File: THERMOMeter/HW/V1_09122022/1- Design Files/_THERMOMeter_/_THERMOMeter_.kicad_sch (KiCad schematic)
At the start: 0 parts

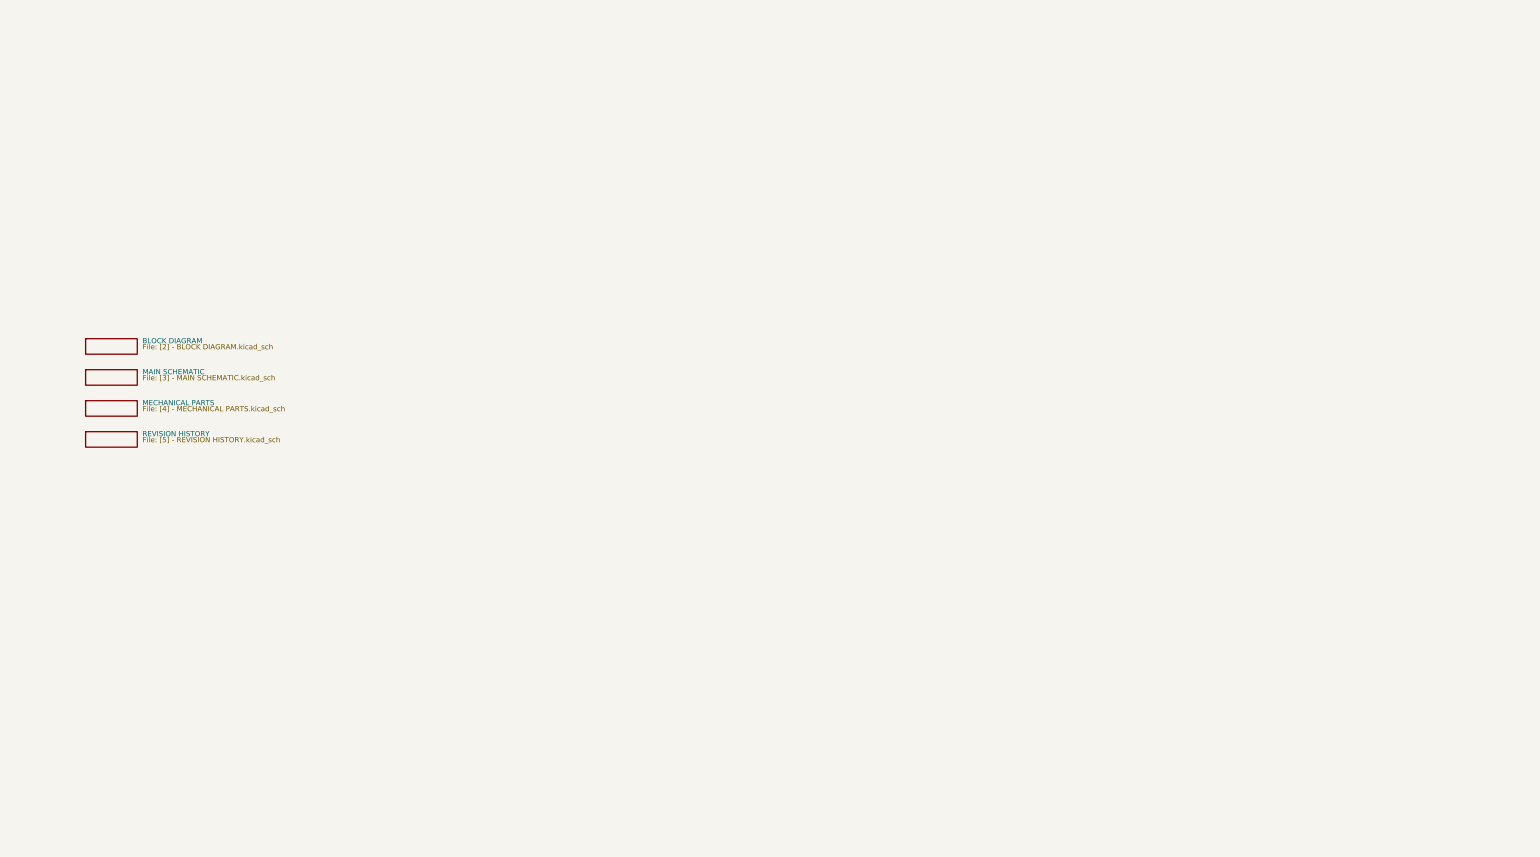
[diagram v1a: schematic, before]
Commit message: hardware template has been modified
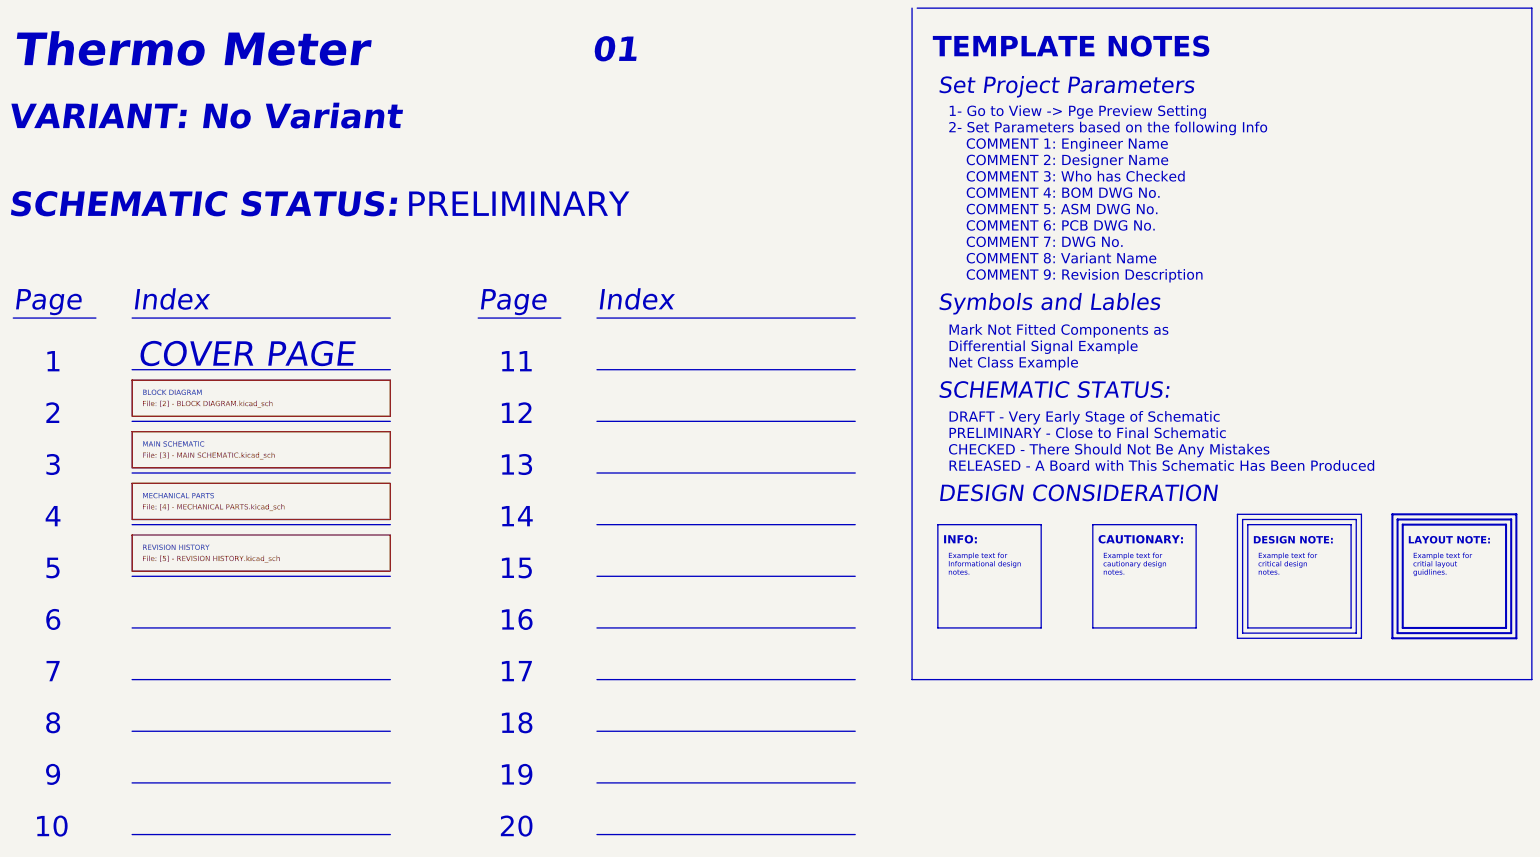
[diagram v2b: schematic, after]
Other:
- note added: "${ISSUE_DATE}"
- note added: "${REVISION}"
- note added: "${TITLE}"
- note added: "1"
- note added: "1- Go to View -> Pge Preview Setting 2- Set Parameters based on the following Info COMMENT 1: Engineer Name COMMENT 2: Designer Name COMMENT 3: Who has Checked COMMENT 4: BOM DWG No. COMMENT 5: ASM DWG No. COMMENT 6: PCB DWG No. COMMENT 7: DWG No. COMMENT 8: Variant Name COMMENT 9: Revision Description"
- note added: "10"
- note added: "11"
- note added: "12"
- note added: "13"
- note added: "14"
- note added: "15"
- note added: "16"
- note added: "17"
- note added: "18"
- note added: "19"
- note added: "2"
- note added: "20"
- note added: "3"
- note added: "4"
- note added: "5"
- note added: "6"
- note added: "7"
- note added: "8"
- note added: "9"
- note added: "CAUTIONARY:"
- note added: "COVER PAGE"
- note added: "DESIGN CONSIDERATION"
- note added: "DESIGN NOTE:"
- note added: "DRAFT - Very Early Stage of Schematic PRELIMINARY - Close to Final Schematic CHECKED - There Should Not Be Any Mistakes RELEASED - A Board with This Schematic Has Been Produced"
- note added: "Example text for Informational design notes."
- note added: "Example text for cautionary design notes."
- note added: "Example text for critial layout guidlines."
- note added: "Example text for critical design notes."
- note added: "INFO:"
- note added: "Index"
- note added: "LAYOUT NOTE:"
- note added: "Mark Not Fitted Components as Differential Signal Example Net Class Example"
- note added: "PRELIMINARY"
- note added: "Page"
- note added: "SCHEMATIC STATUS:"
- note added: "Set Project Parameters"
- note added: "Symbols and Lables"
- note added: "TEMPLATE NOTES"
- note added: "VARIANT: ${COMMENT8}"
